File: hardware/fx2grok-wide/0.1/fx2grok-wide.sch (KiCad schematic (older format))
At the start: 43 parts, among them IC1 CY7C68013A-56, J1 Conn_02x05_Odd_Even, J2 Conn_02x05_Odd_Even, P1 pkl_USB_OTG, U1 3.3V, U2 USBLC6-2, U3 DSILC6-4, U4 DSILC6-4, U5 pkl_24LC00, U6 DSILC6-4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

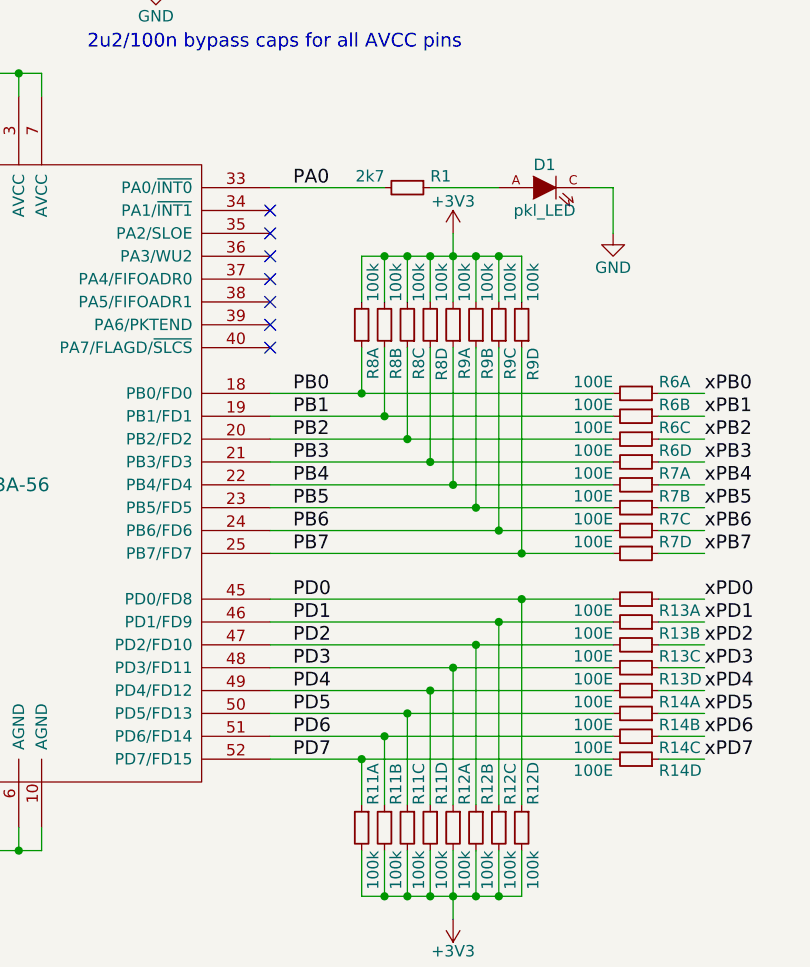
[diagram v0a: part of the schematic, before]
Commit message: Switch the LED to PA1, and start laying out the PCB.
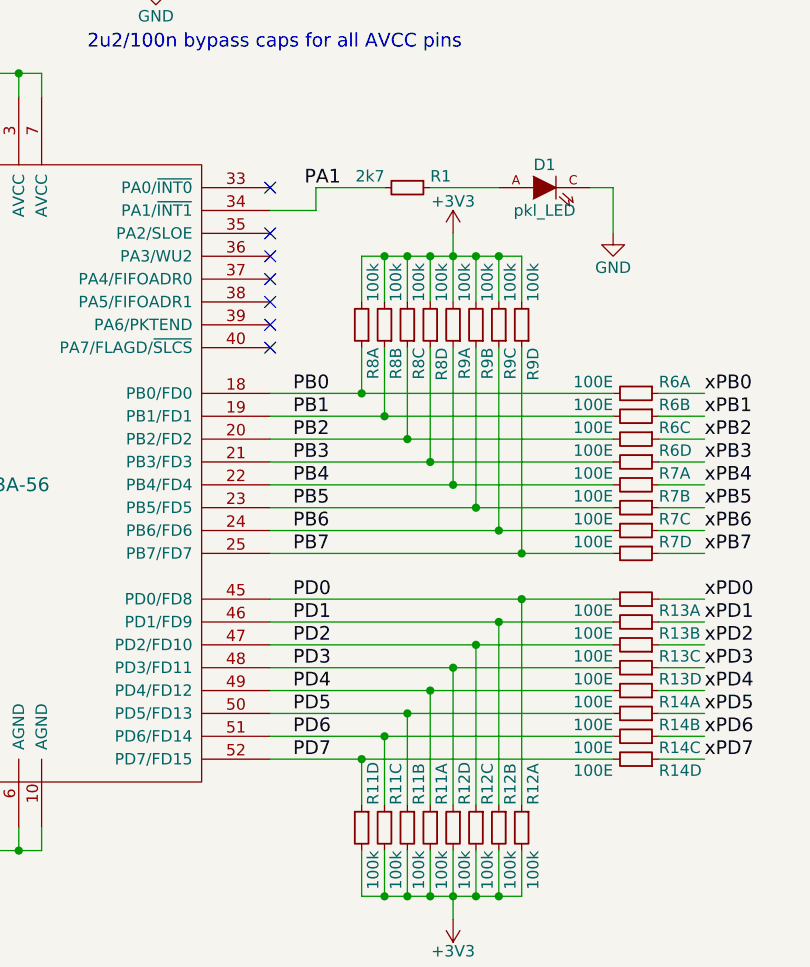
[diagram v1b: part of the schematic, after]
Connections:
- net PD0: now also R12.1; no longer R12.7
- net PD1: now also R12.3; no longer R12.5
- net PD2: now also R12.5; no longer R12.3
- net PD3: now also R12.7; no longer R12.1
- net PD4: now also R11.1; no longer R11.7
- net PD5: now also R11.3; no longer R11.5
- net PD6: now also R11.5; no longer R11.3
- net PD7: now also R11.7; no longer R11.1
- net at IC1.34 (PA1/~INT1): now also R1.2
- net PA0: no longer names the net of IC1.33 (PA0/~INT0)
- net PA0: no longer R1.2
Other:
- moved on the sheet: R11A, R11B, R11C, R11D, R12A, R12B, R12C, R12D
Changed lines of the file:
@@
 LIBS:contrib
 LIBS:valves
-LIBS:fx2grok-flat-cache
+LIBS:pkl_conn
+LIBS:pkl_cypress
+LIBS:pkl_device
+LIBS:pkl_ftdi
+LIBS:pkl_lattice
+LIBS:pkl_linear
+LIBS:pkl_logos
+LIBS:pkl_maxim
+LIBS:pkl_memory
+LIBS:pkl_misc
+LIBS:pkl_molex
+LIBS:pkl_power
+LIBS:pkl_sensor
+LIBS:pkl_silabs
+LIBS:pkl_tag_connect
+LIBS:pkl_texas
+LIBS:fx2grok-wide-cache
 EELAYER 25 0
 EELAYER END
@@
 NoConn ~ 4200 3900
 NoConn ~ 4200 4000
-NoConn ~ 6900 2400
 NoConn ~ 6900 2500
 NoConn ~ 6900 2600
@@
 NoConn ~ 6900 2900
 NoConn ~ 6900 3000
-Wire Wire Line
-	6900 2300 7400 2300
-Text Label 7000 2300 0    60   ~ 0
-PA0
+Text Label 7050 2300 0    60   ~ 0
+PA1
 Wire Wire Line
 	6900 3200 8400 3200
@@
 L pkl_R4_Small R11
 U 1 1 59D4F446
+P 7600 5100
+F 0 "R11" V 7550 5200 50  0000 L CNN
+F 1 "100k" V 7550 5000 50  0000 R CNN
+F 2 "pkl_dipol:R_Array_Convex_4x0402" H 7600 5100 60  0001 C CNN
+F 3 "" H 7600 5100 60  0000 C CNN
+F 4 "ANY" H 7600 5100 60  0001 C CNN "Source"
+	1    7600 5100
+	-1   0    0    -1
+$EndComp
+$Comp
+L pkl_R4_Small R11
+U 2 1 59D4F44D
+P 7500 5100
+F 0 "R11" V 7450 5200 50  0000 L CNN
+F 1 "100k" V 7450 5000 50  0000 R CNN
+F 2 "pkl_dipol:R_Array_Convex_4x0402" H 7500 5100 60  0001 C CNN
+F 3 "" H 7500 5100 60  0000 C CNN
+F 4 "ANY" H 7500 5100 60  0001 C CNN "Source"
+	2    7500 5100
+	-1   0    0    -1
+$EndComp
+$Comp
+L pkl_R4_Small R11
+U 3 1 59D4F454
+P 7400 5100
+F 0 "R11" V 7350 5200 50  0000 L CNN
+F 1 "100k" V 7350 5000 50  0000 R CNN
+F 2 "pkl_dipol:R_Array_Convex_4x0402" H 7400 5100 60  0001 C CNN
+F 3 "" H 7400 5100 60  0000 C CNN
+F 4 "ANY" H 7400 5100 60  0001 C CNN "Source"
+	3    7400 5100
+	-1   0    0    -1
+$EndComp
+$Comp
+L pkl_R4_Small R11
+U 4 1 59D4F45B
 P 7300 5100
 F 0 "R11" V 7250 5200 50  0000 L CNN
@@
 F 3 "" H 7300 5100 60  0000 C CNN
 F 4 "ANY" H 7300 5100 60  0001 C CNN "Source"
-	1    7300 5100
-	-1   0    0    -1
-$EndComp
-$Comp
-L pkl_R4_Small R11
-U 2 1 59D4F44D
-P 7400 5100
-F 0 "R11" V 7350 5200 50  0000 L CNN
-F 1 "100k" V 7350 5000 50  0000 R CNN
-F 2 "pkl_dipol:R_Array_Convex_4x0402" H 7400 5100 60  0001 C CNN
-F 3 "" H 7400 5100 60  0000 C CNN
-F 4 "ANY" H 7400 5100 60  0001 C CNN "Source"
-	2    7400 5100
-	-1   0    0    -1
-$EndComp
-$Comp
-L pkl_R4_Small R11
-U 3 1 59D4F454
-P 7500 5100
-F 0 "R11" V 7450 5200 50  0000 L CNN
-F 1 "100k" V 7450 5000 50  0000 R CNN
-F 2 "pkl_dipol:R_Array_Convex_4x0402" H 7500 5100 60  0001 C CNN
-F 3 "" H 7500 5100 60  0000 C CNN
-F 4 "ANY" H 7500 5100 60  0001 C CNN "Source"
-	3    7500 5100
-	-1   0    0    -1
-$EndComp
-$Comp
-L pkl_R4_Small R11
-U 4 1 59D4F45B
-P 7600 5100
-F 0 "R11" V 7550 5200 50  0000 L CNN
-F 1 "100k" V 7550 5000 50  0000 R CNN
-F 2 "pkl_dipol:R_Array_Convex_4x0402" H 7600 5100 60  0001 C CNN
-F 3 "" H 7600 5100 60  0000 C CNN
-F 4 "ANY" H 7600 5100 60  0001 C CNN "Source"
-	4    7600 5100
+	4    7300 5100
 	-1   0    0    -1
 $EndComp
@@
 L pkl_R4_Small R12
 U 1 1 59D4F462
+P 8000 5100
+F 0 "R12" V 7950 5200 50  0000 L CNN
+F 1 "100k" V 7950 5000 50  0000 R CNN
+F 2 "pkl_dipol:R_Array_Convex_4x0402" H 8000 5100 60  0001 C CNN
+F 3 "" H 8000 5100 60  0000 C CNN
+F 4 "ANY" H 8000 5100 60  0001 C CNN "Source"
+	1    8000 5100
+	-1   0    0    -1
+$EndComp
+$Comp
+L pkl_R4_Small R12
+U 2 1 59D4F469
+P 7900 5100
+F 0 "R12" V 7850 5200 50  0000 L CNN
+F 1 "100k" V 7850 5000 50  0000 R CNN
+F 2 "pkl_dipol:R_Array_Convex_4x0402" H 7900 5100 60  0001 C CNN
+F 3 "" H 7900 5100 60  0000 C CNN
+F 4 "ANY" H 7900 5100 60  0001 C CNN "Source"
+	2    7900 5100
+	-1   0    0    -1
+$EndComp
+$Comp
+L pkl_R4_Small R12
+U 3 1 59D4F470
+P 7800 5100
+F 0 "R12" V 7750 5200 50  0000 L CNN
+F 1 "100k" V 7750 5000 50  0000 R CNN
+F 2 "pkl_dipol:R_Array_Convex_4x0402" H 7800 5100 60  0001 C CNN
+F 3 "" H 7800 5100 60  0000 C CNN
+F 4 "ANY" H 7800 5100 60  0001 C CNN "Source"
+	3    7800 5100
+	-1   0    0    -1
+$EndComp
+$Comp
+L pkl_R4_Small R12
+U 4 1 59D4F477
 P 7700 5100
 F 0 "R12" V 7650 5200 50  0000 L CNN
@@
 F 3 "" H 7700 5100 60  0000 C CNN
 F 4 "ANY" H 7700 5100 60  0001 C CNN "Source"
-	1    7700 5100
-	-1   0    0    -1
-$EndComp
-$Comp
-L pkl_R4_Small R12
-U 2 1 59D4F469
-P 7800 5100
-F 0 "R12" V 7750 5200 50  0000 L CNN
-F 1 "100k" V 7750 5000 50  0000 R CNN
-F 2 "pkl_dipol:R_Array_Convex_4x0402" H 7800 5100 60  0001 C CNN
-F 3 "" H 7800 5100 60  0000 C CNN
-F 4 "ANY" H 7800 5100 60  0001 C CNN "Source"
-	2    7800 5100
-	-1   0    0    -1
-$EndComp
-$Comp
-L pkl_R4_Small R12
-U 3 1 59D4F470
-P 7900 5100
-F 0 "R12" V 7850 5200 50  0000 L CNN
-F 1 "100k" V 7850 5000 50  0000 R CNN
-F 2 "pkl_dipol:R_Array_Convex_4x0402" H 7900 5100 60  0001 C CNN
-F 3 "" H 7900 5100 60  0000 C CNN
-F 4 "ANY" H 7900 5100 60  0001 C CNN "Source"
-	3    7900 5100
-	-1   0    0    -1
-$EndComp
-$Comp
-L pkl_R4_Small R12
-U 4 1 59D4F477
-P 8000 5100
-F 0 "R12" V 7950 5200 50  0000 L CNN
-F 1 "100k" V 7950 5000 50  0000 R CNN
-F 2 "pkl_dipol:R_Array_Convex_4x0402" H 8000 5100 60  0001 C CNN
-F 3 "" H 8000 5100 60  0000 C CNN
-F 4 "ANY" H 8000 5100 60  0001 C CNN "Source"
-	4    8000 5100
+	4    7700 5100
 	-1   0    0    -1
 $EndComp
@@
 	8000 5000 8000 4100
 Connection ~ 8000 4100
+Wire Wire Line
+	7400 2300 7100 2300
+Wire Wire Line
+	7100 2300 7100 2400
+Wire Wire Line
+	7100 2400 6900 2400
+NoConn ~ 6900 2300
 $EndSCHEMATC

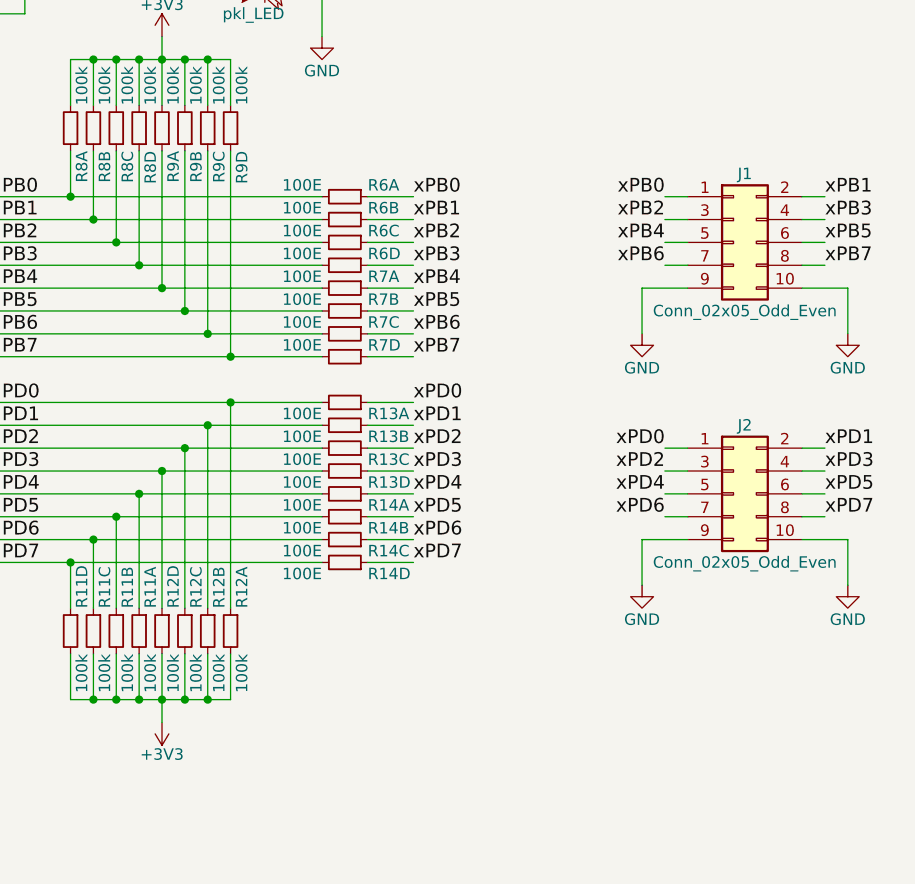
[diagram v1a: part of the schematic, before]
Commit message: Switch to a different footprint for the FX2, and make the input connectors SMD pads on both sides of the PCB(Can stick a 2x5 through-hole header over the side of the PCB and solder it on). Made a bunch of progress on laying out the PCB, currently ~1.5sqin. Not particularly happy with how the inputs come out on opposite ends of the thing, but that's how the chip wants them to be laid out.
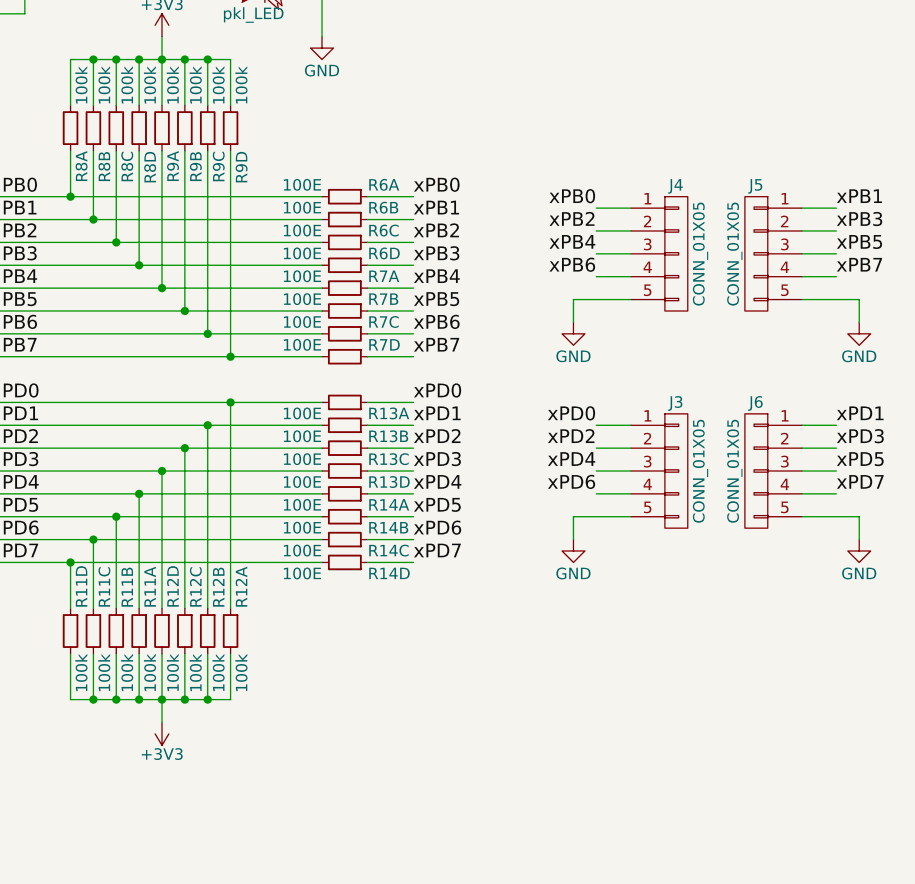
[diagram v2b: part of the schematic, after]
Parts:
- removed J1, J2: Conn_02x05_Odd_Even, pkl_samtec:FTSH-105-XX-X-DV, symbol Conn_02x05_Odd_Even
- added J3, J4, J5, J6: CONN_01X05, izzy:Pin_Header_Angled_1x05_Pitch1.27mm_SMD, symbol CONN_01X05
- IC1: footprint pkl_housings_dfn_qfn:QFN-56-1EP_8x8mm_Pitch0.5mm -> izzy:QFN-56-1EP_8x8mm_Pitch0.5mm-novias
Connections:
- net GND: now also J3.5 (P5), J4.5 (P5), J5.5 (P5), J6.5 (P5)
- net xPB0: now also J4.1 (P1)
- net xPB1: now also J5.1 (P1)
- net xPB2: now also J4.2 (P2)
- net xPB3: now also J5.2 (P2)
- net xPB4: now also J4.3 (P3)
- net xPB5: now also J5.3 (P3)
- net xPB6: now also J4.4 (P4)
- net xPB7: now also J5.4 (P4)
- net xPD0: now also J3.1 (P1)
- net xPD1: now also J6.1 (P1)
- net xPD2: now also J3.2 (P2)
- net xPD3: now also J6.2 (P2)
- net xPD4: now also J3.3 (P3)
- net xPD5: now also J6.3 (P3)
- net xPD6: now also J3.4 (P4)
- net xPD7: now also J6.4 (P4)

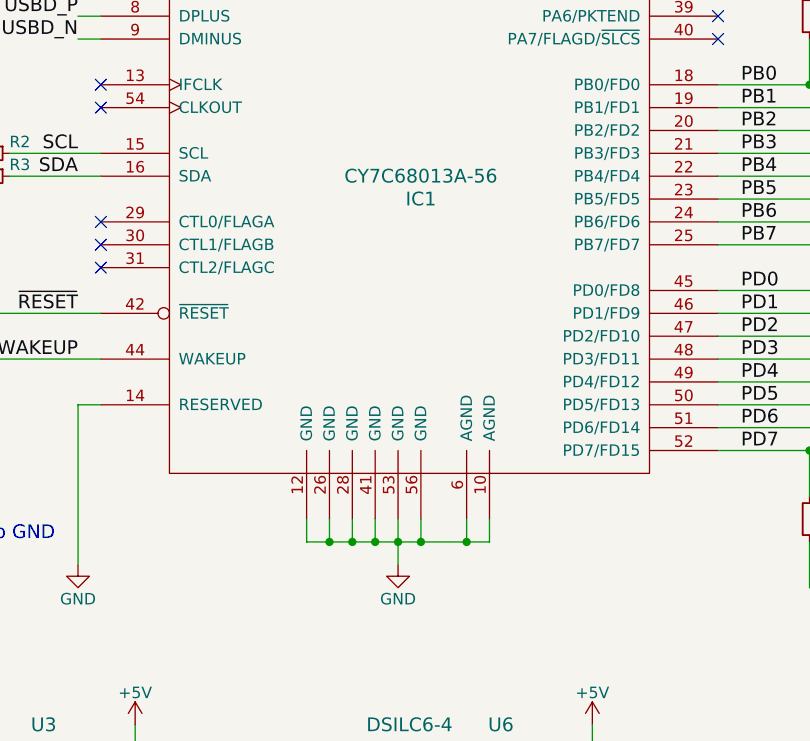
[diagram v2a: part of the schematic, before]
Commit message: Switch back to the old FX2 footprint, add the center pad of the QFN to the schematic symbol, and connect it to ground as recommended by Cypress. And connect a few more traces.
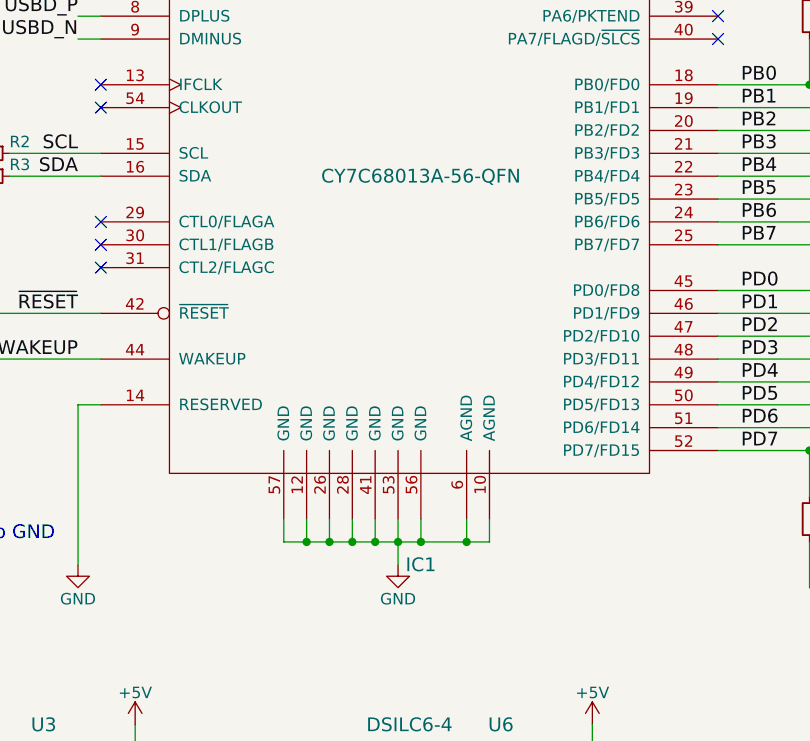
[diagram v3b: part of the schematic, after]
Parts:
- removed IC1: CY7C68013A-56, izzy:QFN-56-1EP_8x8mm_Pitch0.5mm-novias, symbol CY7C68013A-56
- added IC1: CY7C68013A-56-QFN, pkl_housings_dfn_qfn:QFN-56-1EP_8x8mm_Pitch0.5mm, symbol CY7C68013A-56-QFN
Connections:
- net +3V3: now also IC1.11 (VCC), IC1.17 (VCC), IC1.27 (VCC), IC1.3 (AVCC), IC1.32 (VCC), IC1.43 (VCC), IC1.55 (VCC), IC1.7 (AVCC)
- net GND: now also IC1.10 (AGND), IC1.12 (GND), IC1.14 (RESERVED), IC1.26 (GND), IC1.28 (GND), IC1.41 (GND), IC1.53 (GND), IC1.56 (GND), IC1.57 (GND), IC1.6 (AGND)
- net PB0: now also IC1.18 (PB0/FD0)
- net PB1: now also IC1.19 (PB1/FD1)
- net PB2: now also IC1.20 (PB2/FD2)
- net PB3: now also IC1.21 (PB3/FD3)
- net PB4: now also IC1.22 (PB4/FD4)
- net PB5: now also IC1.23 (PB5/FD5)
- net PB6: now also IC1.24 (PB6/FD6)
- net PB7: now also IC1.25 (PB7/FD7)
- net PD0: now also IC1.45 (PD0/FD8)
- net PD1: now also IC1.46 (PD1/FD9)
- net PD2: now also IC1.47 (PD2/FD10)
- net PD3: now also IC1.48 (PD3/FD11)
- net PD4: now also IC1.49 (PD4/FD12)
- net PD5: now also IC1.50 (PD5/FD13)
- net PD6: now also IC1.51 (PD6/FD14)
- net PD7: now also IC1.52 (PD7/FD15)
- net SCL: now also IC1.15 (SCL)
- net SDA: now also IC1.16 (SDA)
- net USBD_N: now also IC1.9 (DMINUS)
- net USBD_P: now also IC1.8 (DPLUS)
- net WAKEUP: now also IC1.44 (WAKEUP)
- net XTALIN: now also IC1.5 (XTALIN)
- net XTALOUT: now also IC1.4 (XTALOUT)
- net ~RESET: now also IC1.42 (~RESET)
- net at R1.2: now also IC1.34 (PA1/~INT1)
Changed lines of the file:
@@
 $EndDescr
-$Comp
-L CY7C68013A-56 IC1
-U 1 1 59BC7288
-P 5600 3600
-F 0 "IC1" H 5600 3500 60  0000 C CNN
-F 1 "CY7C68013A-56" H 5600 3600 60  0000 C CNN
-F 2 "izzy:QFN-56-1EP_8x8mm_Pitch0.5mm-novias" H 5600 3600 60  0001 C CNN
-F 3 "" H 5600 3600 60  0001 C CNN
-	1    5600 3600
-	1    0    0    -1
-$EndComp
 $Comp
 L pkl_USB_OTG P1
@@
 	5100 5100 5100 5200
 Wire Wire Line
-	5100 5200 5900 5200
+	5000 5200 5900 5200
 Wire Wire Line
 	5900 5200 5900 5100
@@
 Wire Wire Line
 	10750 3650 10750 3750
+$Comp
+L CY7C68013A-56-QFN IC1
+U 1 1 59D7E612
+P 5600 3600
+F 0 "IC1" H 5600 1900 60  0000 C CNN
+F 1 "CY7C68013A-56-QFN" H 5600 3600 60  0000 C CNN
+F 2 "pkl_housings_dfn_qfn:QFN-56-1EP_8x8mm_Pitch0.5mm" H 5600 3600 60  0001 C CNN
+F 3 "" H 5600 3600 60  0001 C CNN
+	1    5600 3600
+	1    0    0    -1
+$EndComp
+Wire Wire Line
+	5000 5200 5000 5100
+Connection ~ 5100 5200
 $EndSCHEMATC
